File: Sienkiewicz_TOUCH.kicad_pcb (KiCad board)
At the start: 2 copper layers, 38 x 38 mm, 21 parts, among them J1 Conn_ARM_SWD_TagConnect_TC203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, J2 USB4135-GF-A_REVA, U1 ATtiny204-SS, U2 AT42QT1012-T

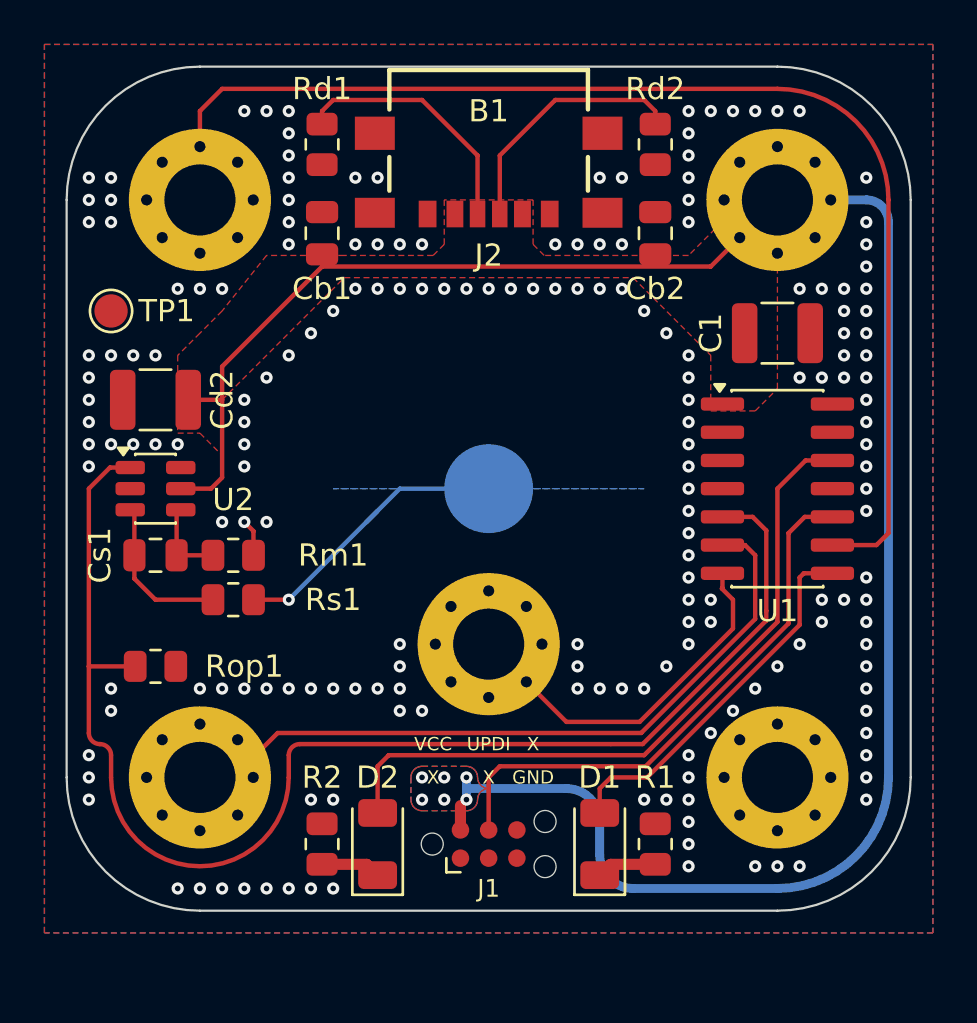
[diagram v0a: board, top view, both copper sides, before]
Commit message: screw interface update - changed pinout
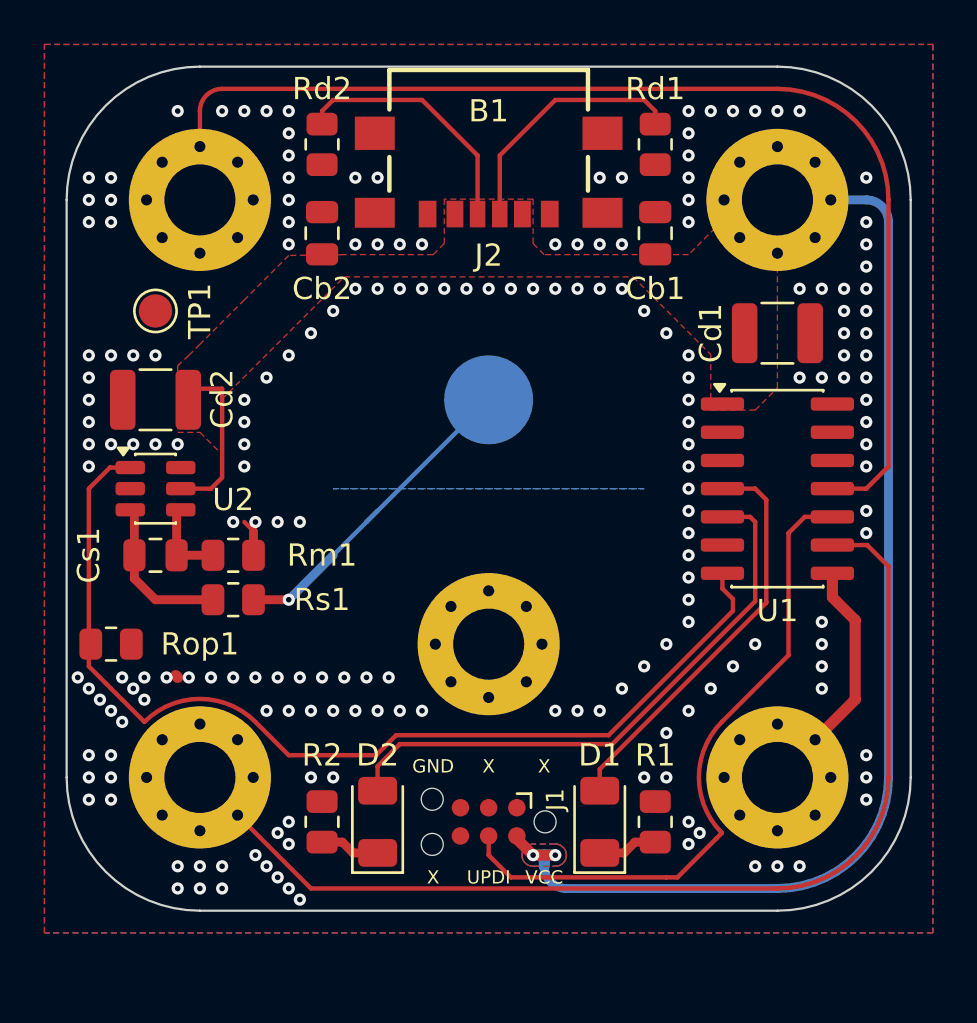
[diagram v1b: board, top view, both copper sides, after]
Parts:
- moved Cb1 15.0 mm to (156.0, 78.5)
- moved Cb2 15.0 mm to (141.0, 78.5)
- moved Rd1 15.0 mm to (156.0, 74.5)
- moved Rd2 15.0 mm to (141.0, 74.5)
- moved TouP1 4.00 mm to (148.5, 86.0)
- moved Rop1 2.24 mm to (131.5, 97.0)
- moved TP1 2.00 mm to (133.5, 82.0)
- moved D1 1.00 mm to (153.5, 105.0)
- moved D2 1.00 mm to (143.5, 105.0)
- moved J1 1.00 mm to (148.5, 105.0), turned to 180 degrees
- moved R1 1.00 mm to (156.0, 105.0)
- moved R2 1.00 mm to (141.0, 105.0)
- renumbered C1 to Cd1
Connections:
- B1 pad 3: GND -> /Project Architecture/Section B - uC/SR_LATCH
- B1 pad 5: /Project Architecture/Section B - uC/SR_LATCH -> GND
- Rd1 pad 1: Net-(J2-VCONN) -> Net-(J2-CC)
- Rd2 pad 1: Net-(J2-CC) -> Net-(J2-VCONN)
- U1 pad 11: unconnected-(U1-PA1-Pad11) -> /Project Architecture/Section B - uC/SR_SDI
- U1 pad 12: LED2 -> unconnected-(U1-PA2-Pad12)
- U1 pad 4: unconnected-(U1-PA6-Pad4) -> LED1
- U1 pad 5: /Project Architecture/Section B - uC/TT -> LED2
- U1 pad 6: /Project Architecture/Section B - uC/SR_CLK -> unconnected-(U1-PB3-Pad6)
- U1 pad 7: /Project Architecture/Section B - uC/SR_LATCH -> /Project Architecture/Section B - uC/TT
- U1 pad 8: LED1 -> /Project Architecture/Section B - uC/SR_LATCH
- U1 pad 9: /Project Architecture/Section B - uC/SR_SDI -> /Project Architecture/Section B - uC/SR_CLK
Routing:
- net VCC: track 83.1 -> 52.6 mm, vias 6 -> 2
- net /Project Architecture/Section B - uC/SR_CLK: track 32.5 -> 42.0 mm
- net /Project Architecture/Section B - uC/SR_LATCH: track 19.9 -> 12.1 mm
- net /Project Architecture/Section B - uC/TT: track 46.9 -> 40.5 mm
- net LED2: track 31.8 -> 26.3 mm
- net /Project Architecture/Section B - uC/SR_SDI: track 47.6 -> 43.9 mm
- net GND: track 1.67 -> 4.79 mm, vias 186 -> 193
- net /Project Architecture/Section C - Touch sensor/TOUCH: track 13.4 -> 16.0 mm
- net LED1: track 16.8 -> 18.4 mm
- net Net-(D1-K): track 3.30 -> 2.70 mm

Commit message: refresh
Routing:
- net GND: track 4.79 -> 6.47 mm, vias 193 -> 198
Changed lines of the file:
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@@
+	)
+	(segment
+		(start 132.4125 98.0875)
+		(end 132 98.5)
+		(width 0.4)
+		(layer "F.Cu")
+		(net 1)
 	)
 	(segment
@@
 		(net 1)
 	)
+	(segment
+		(start 132.4125 97)
+		(end 132.4125 98.0875)
+		(width 0.4)
+		(layer "F.Cu")
+		(net 1)
+	)
 	(via
 		(at 164.5 82)
@@
 	)
 	(via
+		(at 130.5 82)
+		(size 0.55)
+		(drill 0.25)
+		(layers "F.Cu" "B.Cu")
+		(free yes)
+		(net 1)
+	)
+	(via
 		(at 143.5 81)
 		(size 0.55)
@@
 	)
 	(via
-		(at 133.5 84)
-		(size 0.55)
-		(drill 0.25)
-		(layers "F.Cu" "B.Cu")
-		(free yes)
-		(net 1)
-	)
-	(via
 		(at 165.5 91)
 		(size 0.55)
@@
 	)
 	(via
+		(at 130.5 81)
+		(size 0.55)
+		(drill 0.25)
+		(layers "F.Cu" "B.Cu")
+		(free yes)
+		(net 1)
+	)
+	(via
 		(at 141.5 82)
 		(size 0.55)
@@
 	)
 	(via
+		(at 130.5 80)
+		(size 0.55)
+		(drill 0.25)
+		(layers "F.Cu" "B.Cu")
+		(free yes)
+		(net 1)
+	)
+	(via
 		(at 133 99.5)
 		(size 0.55)
@@
 	)
 	(via
+		(at 131.5 80)
+		(size 0.55)
+		(drill 0.25)
+		(layers "F.Cu" "B.Cu")
+		(free yes)
+		(net 1)
+	)
+	(via
 		(at 150.5 81)
 		(size 0.55)
@@
 	)
 	(via
+		(at 130.5 83)
+		(size 0.55)
+		(drill 0.25)
+		(layers "F.Cu" "B.Cu")
+		(free yes)
+		(net 1)
+	)
+	(via
 		(at 135.5 108)
 		(size 0.55)
@@
 		(size 0.55)
 		(drill 0.25)
+		(layers "F.Cu" "B.Cu")
+		(free yes)
+		(net 1)
+	)
+	(via
+		(at 132.5 80)
+		(size 0.55)
+		(drill 0.25)

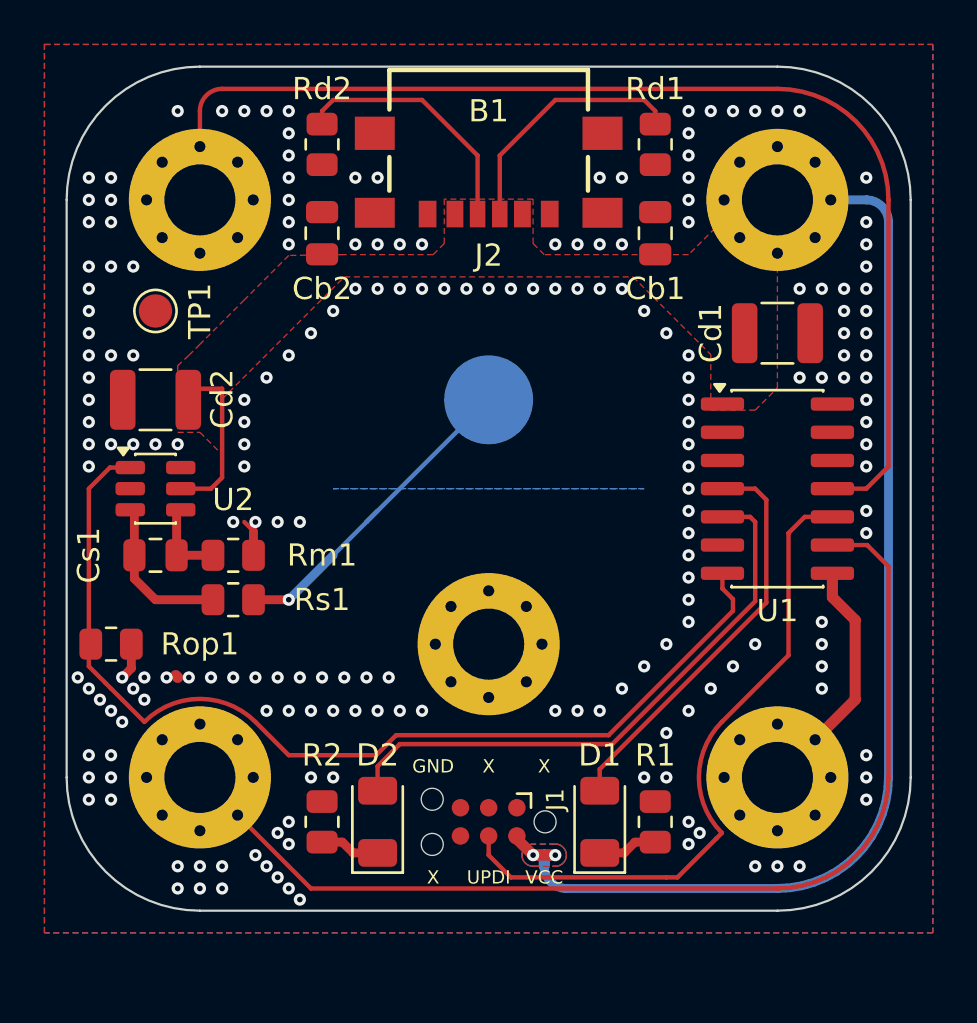
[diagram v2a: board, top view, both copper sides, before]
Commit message: bom update, qr-code added
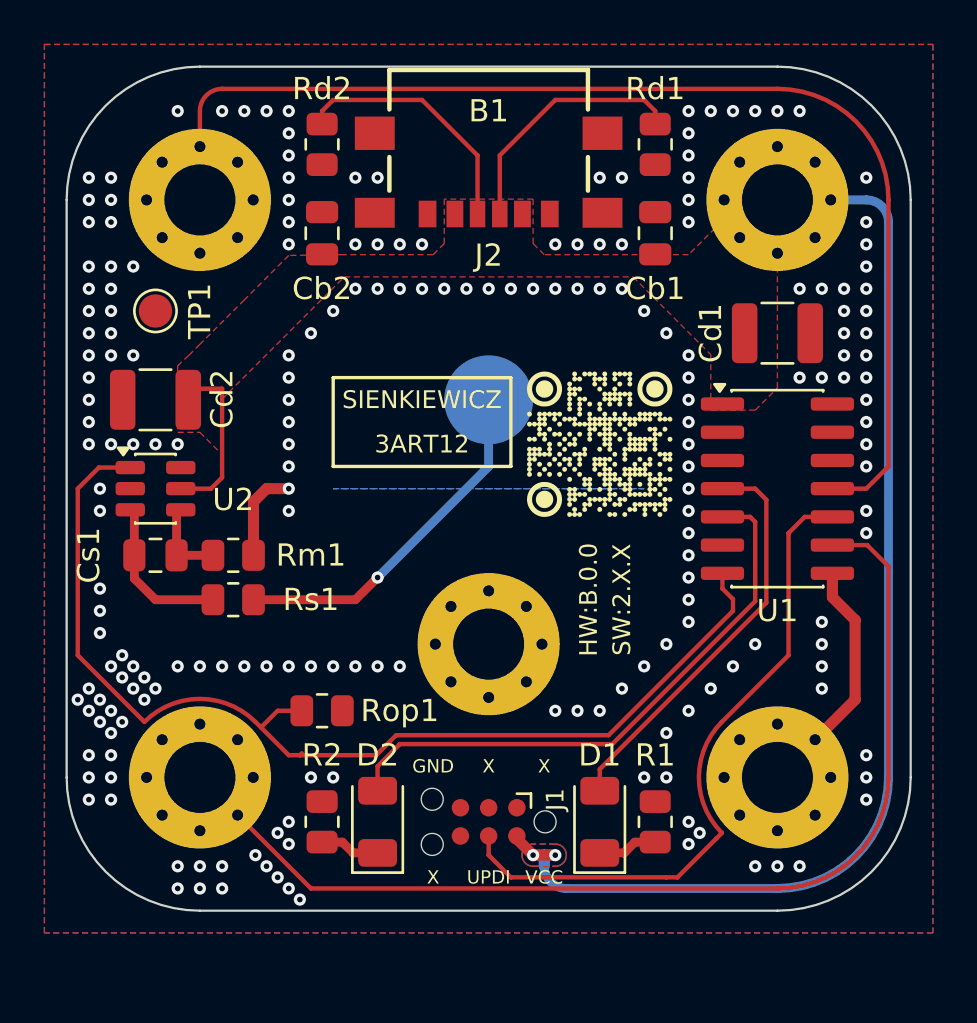
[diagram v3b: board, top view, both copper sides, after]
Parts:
- added G***: LOGO, __QR__Github.Sienkiewicz_TOUCH:QR__Github.Sienkiewicz_TOUCH, F.Cu at (153.5, 88.0)
- J1: value Conn_ARM_SWD_TagConnect_TC2030-NL -> TC2030-NL
- moved Rop1 9.96 mm to (141.0, 100.0)
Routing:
- net /Project Architecture/Section B - uC/TT: track 40.5 -> 43.5 mm
- net GND: track 6.47 -> 7.24 mm, vias 198 -> 202
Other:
- board text added: "3ART12"
- board text added: "HW:B.0.0"
- board text added: "SIENKIEWICZ"
- board text added: "SW:2.X.X"

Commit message: [sch] added R3 to prevent high current drain from cap touch chip
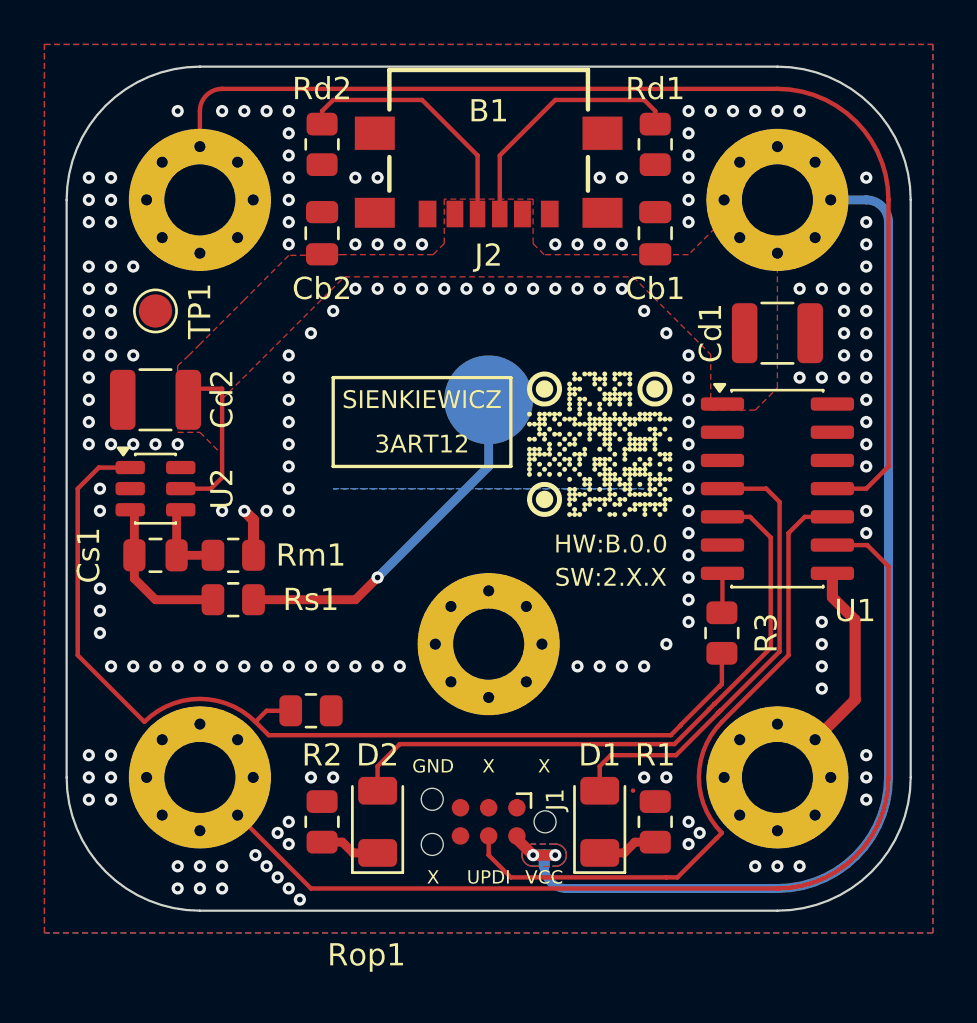
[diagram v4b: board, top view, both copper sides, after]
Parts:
- added R3: 1k, Resistor_SMD:R_0805_2012Metric, F.Cu at (159.0, 96.5)
- Cs1: value 2n2 -> 2n7
- J1: value TC2030-NL -> Conn_ARM_SWD_TagConnect_TC2030-NL
- Rs1: value 4k3 -> 5k1
- U1: value ATtiny204-SS -> ATtiny204
- moved Rop1 0.50 mm to (140.5, 100.0)
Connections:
- U1 pad 7: /Project Architecture/Section B - uC/TT -> /Project Architecture/Section B - uC/TT_uC
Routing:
- net /Project Architecture/Section B - uC/TT: track 43.5 -> 39.9 mm
- net LED1: track 18.4 -> 21.1 mm
- net LED2: track 26.3 -> 28.5 mm
- net GND: track 7.24 -> 5.17 mm, vias 202 -> 186
- net /Project Architecture/Section B - uC/TT_uC: track 0.00 -> 1.79 mm

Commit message: [pcb] board outline/connection changed / back compatibility not possible
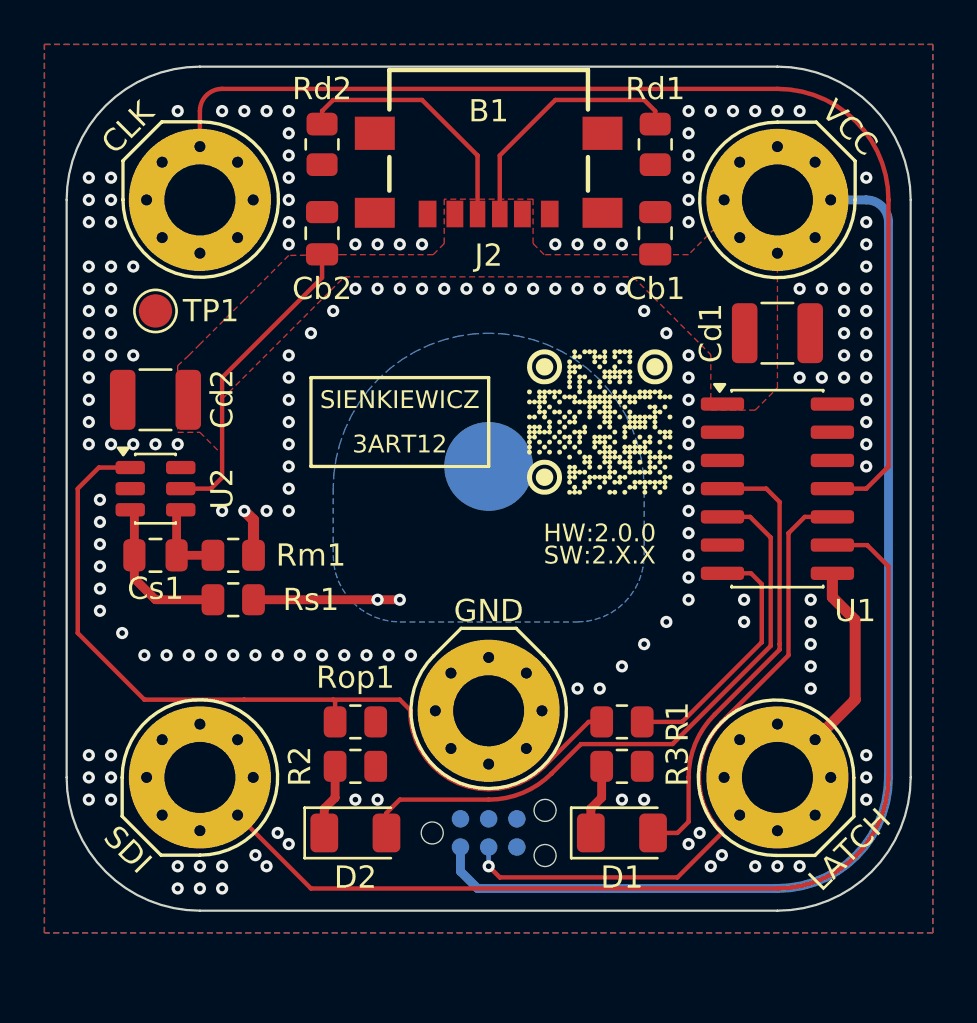
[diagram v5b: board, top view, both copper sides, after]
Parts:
- added REF**: KiCad-Logo2_5mm_SilkScreen, Symbol:KiCad-Logo2_5mm_SilkScreen, B.Cu at (148.5, 75.0)
- J1: moved to B.Cu
- U1: value ATtiny204 -> ATtiny204-SS
- moved R3 6.02 mm to (154.5, 100.5), turned to 0 degrees
- moved TouP1 3.00 mm to (148.5, 89.0)
- moved R1 2.92 mm to (154.5, 102.5), turned to 0 degrees
- moved R2 2.92 mm to (142.5, 102.5), turned to 0 degrees
- moved Rop1 2.06 mm to (142.5, 100.5)
- moved D1 1.12 mm to (154.5, 105.5), turned to 0 degrees
- moved D2 1.12 mm to (142.5, 105.5), turned to 0 degrees
- moved G*** 1.00 mm to (153.5, 87.0)
- moved J1 0.50 mm to (148.5, 105.5), turned to 0 degrees
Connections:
- B1 pad 1: /Project Architecture/Section B - uC/SR_SDI -> /Project Architecture/Section B - uC/SR_CLK
- B1 pad 4: /Project Architecture/Section B - uC/SR_CLK -> /Project Architecture/Section B - uC/SR_SDI
- U1 pad 11: /Project Architecture/Section B - uC/SR_SDI -> /Project Architecture/Section B - uC/SR_CLK
- U1 pad 9: /Project Architecture/Section B - uC/SR_CLK -> /Project Architecture/Section B - uC/SR_SDI
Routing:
- net /Project Architecture/Section B - uC/TT: track 39.9 -> 30.2 mm
- net /Project Architecture/Section B - uC/TT_uC: track 1.79 -> 11.5 mm
- net /Project Architecture/Section C - Touch sensor/TOUCH: track 16.1 -> 6.59 mm, vias 1 -> 2
- net VCC: track 52.6 -> 61.6 mm, vias 2 -> 0
- net LED1: track 21.1 -> 17.8 mm
- net LED2: track 28.5 -> 25.4 mm
- net /Project Architecture/Section B - uC/SR_SDI: track 43.9 -> 42.0 mm
- net /Project Architecture/Section B - uC/SR_CLK: track 42.0 -> 43.9 mm
- net /Project Architecture/Section B - uC/UPDI: track 25.9 -> 25.7 mm, vias 0 -> 1
- net GND: vias 186 -> 180
- removed copper zone on B.Cu, net VCC
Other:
- board text added: "CLK"
- board text added: "HW:2.0.0"
- board text added: "LATCH"
- board text added: "SDI"
- board text removed: "HW:B.0.0"
- board text removed: "UPDI"
